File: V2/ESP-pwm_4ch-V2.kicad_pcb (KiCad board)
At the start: 2 copper layers, 103 x 67.8 mm, 37 parts, among them J1 12VDC, J2 OUT1, J3 OUT2, J4 OUT3, J5 OUT4, Q1 IRLB8721PBF, Q2 IRLB8721PBF, Q3 IRLB8721PBF, Q4 IRLB8721PBF, U1 L78M05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

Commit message: work in progress
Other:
- board text added: "MAX LOAD 5 A PER CHANNEL 16 A TOTAL"
- board text removed: "MAXIMUM 5 A PER CHANNEL 16 A TOTAL"
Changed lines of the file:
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@@
     (fp_arc (start -1.543104 -2.220356) (mid -0.831231 -1.810248) (end -0.550001 -1.038327) (layer "F.SilkS") (width 0.12))
     (fp_arc (start 5.549999 -1.038327) (mid 5.831229 -1.810249) (end 6.543103 -2.220357) (layer "F.SilkS") (width 0.12))
-    (fp_arc (start 0.549998 -1.038327) (mid -0.000002 1.174999) (end -0.550001 -1.038327) (layer "F.SilkS") (width 0.12))
+    (fp_arc (start 0.549998 -1.038327) (mid -0.000001 1.174999) (end -0.550001 -1.038327) (layer "F.SilkS") (width 0.12))
     (fp_arc (start -3.25 -5.15) (mid -2.5 -5.9) (end -1.75 -5.15) (layer "F.SilkS") (width 0.12))
     (fp_arc (start 3.456896 -2.220358) (mid 3.30859 -2.305797) (end 3.25 -2.466613) (layer "F.SilkS") (width 0.12))
@@
     (fp_arc (start 8.4 2.75) (mid 8.136396 3.386396) (end 7.5 3.65) (layer "F.CrtYd") (width 0.05))
     (fp_arc (start 5.4 -0.9) (mid 5.659303 -1.859555) (end 6.502666 -2.385599) (layer "F.CrtYd") (width 0.05))
-    (fp_arc (start 0.4 -0.9) (mid 0.000001 0.984885) (end -0.399999 -0.9) (layer "F.CrtYd") (width 0.05))
+    (fp_arc (start 0.4 -0.9) (mid 0 0.984886) (end -0.399999 -0.9) (layer "F.CrtYd") (width 0.05))
     (fp_arc (start 6.6 -5.2) (mid 7.5 -6.1) (end 8.4 -5.2) (layer "F.CrtYd") (width 0.05))
     (fp_line (start -3.099999 -5.1) (end -3.099999 -2.5) (layer "F.Fab") (width 0.1))
@@
     (fp_arc (start 1.75 -2.466613) (mid 1.69141 -2.305796) (end 1.543103 -2.220357) (layer "F.SilkS") (width 0.12))
     (fp_arc (start 0.549999 -1.038327) (mid 0.831229 -1.810249) (end 1.543103 -2.220357) (layer "F.SilkS") (width 0.12))
-    (fp_arc (start 0.549998 -1.038327) (mid -0.000002 1.174999) (end -0.550001 -1.038327) (layer "F.SilkS") (width 0.12))
+    (fp_arc (start 0.549998 -1.038327) (mid -0.000001 1.174999) (end -0.550001 -1.038327) (layer "F.SilkS") (width 0.12))
     (fp_arc (start 6.75 -5.149999) (mid 7.5 -5.899999) (end 8.25 -5.149999) (layer "F.SilkS") (width 0.12))
     (fp_arc (start -3.25 -5.15) (mid -2.5 -5.9) (end -1.75 -5.15) (layer "F.SilkS") (width 0.12))
@@
     (fp_arc (start -8.4 -5.2) (mid -7.5 -6.1) (end -6.6 -5.2) (layer "F.CrtYd") (width 0.05))
     (fp_arc (start 0.4 -0.9) (mid 0.659303 -1.859555) (end 1.502666 -2.385599) (layer "F.CrtYd") (width 0.05))
-    (fp_arc (start 0.4 -0.9) (mid 0.000001 0.984885) (end -0.399999 -0.9) (layer "F.CrtYd") (width 0.05))
+    (fp_arc (start 0.4 -0.9) (mid 0 0.984886) (end -0.399999 -0.9) (layer "F.CrtYd") (width 0.05))
     (fp_arc (start -4.6 -0.9) (mid -4.340697 -1.859555) (end -3.497334 -2.385599) (layer "F.CrtYd") (width 0.05))
     (fp_arc (start 5.4 -0.9) (mid 5.000001 0.984885) (end 4.600001 -0.9) (layer "F.CrtYd") (width 0.05))
@@
     (fp_arc (start 3.456896 -2.220358) (mid 3.30859 -2.305797) (end 3.25 -2.466613) (layer "F.SilkS") (width 0.12))
     (fp_arc (start 6.75 -2.466613) (mid 6.69141 -2.305796) (end 6.543103 -2.220357) (layer "F.SilkS") (width 0.12))
-    (fp_arc (start 0.549998 -1.038327) (mid -0.000002 1.174999) (end -0.550001 -1.038327) (layer "F.SilkS") (width 0.12))
+    (fp_arc (start 0.549998 -1.038327) (mid -0.000001 1.174999) (end -0.550001 -1.038327) (layer "F.SilkS") (width 0.12))
     (fp_arc (start -1.543103 -2.220357) (mid -1.69141 -2.305796) (end -1.75 -2.466613) (layer "F.SilkS") (width 0.12))
     (fp_arc (start -3.25 -5.15) (mid -2.5 -5.9) (end -1.75 -5.15) (layer "F.SilkS") (width 0.12))
@@
     (fp_arc (start -8.4 -5.2) (mid -7.5 -6.1) (end -6.6 -5.2) (layer "F.CrtYd") (width 0.05))
     (fp_arc (start -1.502666 -2.385599) (mid -0.659303 -1.859555) (end -0.4 -0.9) (layer "F.CrtYd") (width 0.05))
-    (fp_arc (start 0.4 -0.9) (mid 0.000001 0.984885) (end -0.399999 -0.9) (layer "F.CrtYd") (width 0.05))
+    (fp_arc (start 0.4 -0.9) (mid 0 0.984886) (end -0.399999 -0.9) (layer "F.CrtYd") (width 0.05))
     (fp_arc (start -4.6 -0.9) (mid -4.340697 -1.859555) (end -3.497334 -2.385599) (layer "F.CrtYd") (width 0.05))
     (fp_arc (start 0.4 -0.9) (mid 0.659303 -1.859555) (end 1.502666 -2.385599) (layer "F.CrtYd") (width 0.05))
@@
     (tags "capacitor tantalum")
     (property "Case" "1206/3216")
-    (property "JLCPCB BOM" "0")
-    (property "LCSC Part" "")
+    (property "JLCPCB BOM" "1")
+    (property "LCSC Part" "C7176")
     (property "Mfr" "AVX")
-    (property "Mfr PN" "TAJA105K035TNJ")
+    (property "Mfr PN" "TAJA105K035RNJ")
     (property "Sheetfile" "ESP-pwm_4ch-V2.kicad_sch")
     (property "Sheetname" "")
     (property "Technology" "Tantalum")
-    (property "Vendor" "Mouser")
-    (property "Vendor PN" "581-TAJA105K035TNJ")
+    (property "Vendor" "JLCPCB")
+    (property "Vendor PN" "C7176")
     (attr smd)
     (fp_text reference "C5" (at -3.81 0) (layer "F.SilkS")
@@
     (tags "SOIC SO")
     (property "Case" "SOIC-8")
-    (property "JLCPCB BOM" "0")
-    (property "LCSC Part" "")
+    (property "JLCPCB BOM" "1")
+    (property "LCSC Part" "C49058")
     (property "Mfr" "International Rectifier")
     (property "Mfr PN" "IR4427STRPBF\r")
     (property "Sheetfile" "ESP-pwm_4ch-V2.kicad_sch")
     (property "Sheetname" "")
-    (property "Vendor" "Mouser")
-    (property "Vendor PN" "942-IR4427STRPBF\r")
+    (property "Vendor" "JLCPCB")
+    (property "Vendor PN" "C49058")
     (attr smd)
     (fp_text reference "U4" (at 0 -3.4) (layer "F.SilkS")
@@
     (tags "SOIC SO")
     (property "Case" "SOIC-8")
-    (property "JLCPCB BOM" "0")
-    (property "LCSC Part" "")
+    (property "JLCPCB BOM" "1")
+    (property "LCSC Part" "C49058")
     (property "Mfr" "International Rectifier")
     (property "Mfr PN" "IR4427STRPBF\r")
     (property "Sheetfile" "ESP-pwm_4ch-V2.kicad_sch")
     (property "Sheetname" "")
-    (property "Vendor" "Mouser")
-    (property "Vendor PN" "942-IR4427STRPBF\r")
+    (property "Vendor" "JLCPCB")
+    (property "Vendor PN" "C49058")
     (attr smd)
     (fp_text reference "U5" (at 0 -3.4) (layer "F.SilkS")
@@
     (fp_arc (start 1.75 -2.466613) (mid 1.69141 -2.305796) (end 1.543103 -2.220357) (layer "F.SilkS") (width 0.12))
     (fp_arc (start -6.543104 -2.220357) (mid -5.831231 -1.810248) (end -5.550001 -1.038327) (layer "F.SilkS") (width 0.12))
-    (fp_arc (start 0.549998 -1.038327) (mid -0.000002 1.174999) (end -0.550001 -1.038327) (layer "F.SilkS") (width 0.12))
+    (fp_arc (start 0.549998 -1.038327) (mid -0.000001 1.174999) (end -0.550001 -1.038327) (layer "F.SilkS") (width 0.12))
     (fp_arc (start -1.543103 -2.220357) (mid -1.69141 -2.305796) (end -1.75 -2.466613) (layer "F.SilkS") (width 0.12))
     (fp_arc (start -4.450001 -1.038327) (mid -4.168771 -1.810249) (end -3.456897 -2.220357) (layer "F.SilkS") (width 0.12))
@@
     (fp_arc (start -1.509951 -2.38049) (mid -1.57415 -2.412895) (end -1.600006 -2.48) (layer "F.CrtYd") (width 0.05))
     (fp_arc (start -3.399994 -2.48) (mid -3.42585 -2.412895) (end -3.490049 -2.38049) (layer "F.CrtYd") (width 0.05))
-    (fp_arc (start 0.4 -0.9) (mid 0.000001 0.984885) (end -0.399999 -0.9) (layer "F.CrtYd") (width 0.05))
+    (fp_arc (start 0.4 -0.9) (mid 0 0.984886) (end -0.399999 -0.9) (layer "F.CrtYd") (width 0.05))
     (fp_arc (start 3.490049 -2.38049) (mid 3.42585 -2.412895) (end 3.399994 -2.48) (layer "F.CrtYd") (width 0.05))
     (fp_arc (start -6.502666 -2.385599) (mid -5.659303 -1.859555) (end -5.4 -0.9) (layer "F.CrtYd") (width 0.05))
@@
     (tags "capacitor tantalum")
     (property "Case" "1206/3216")
-    (property "JLCPCB BOM" "0")
-    (property "LCSC Part" "")
+    (property "JLCPCB BOM" "1")
+    (property "LCSC Part" "C7176")
     (property "Mfr" "AVX")
-    (property "Mfr PN" "TAJA105K035TNJ")
+    (property "Mfr PN" "TAJA105K035RNJ")
     (property "Sheetfile" "ESP-pwm_4ch-V2.kicad_sch")
     (property "Sheetname" "")
     (property "Technology" "Tantalum")
-    (property "Vendor" "Mouser")
-    (property "Vendor PN" "581-TAJA105K035TNJ")
+    (property "Vendor" "JLCPCB")
+    (property "Vendor PN" "C7176")
     (attr smd)
     (fp_text reference "C7" (at -3.81 0) (layer "F.SilkS")
@@
     (effects (font (size 1.5 1.5) (thickness 0.25)))
   )
-  (gr_text "MAXIMUM 5 A\nPER CHANNEL\n16 A TOTAL" (at 107.315 83.312) (layer "F.SilkS")
+  (gr_text "MAX LOAD 5 A\nPER CHANNEL\n16 A TOTAL" (at 107.315 83.312) (layer "F.SilkS")
     (effects (font (size 1.8 1.6) (thickness 0.3)))
   )

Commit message: wip
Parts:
- removed the REF** at (82.5, 125.7)
- added ?: , Tales:TMaschio_20x6.4mm, F.Cu at (108.0, 94.0)
- added REF**: OSHW-Logo2_14.6x12mm_SilkScreen, Symbol:OSHW-Logo2_14.6x12mm_SilkScreen, F.Cu at (108.0, 83.8)
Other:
- board text added: "MAX LOAD 5A/CHANNEL 16 A TOTAL"
- board text removed: "MAX LOAD 5 A PER CHANNEL 16 A TOTAL"

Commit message: General improvement to the routing
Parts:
- R4, R5, R6, R7: value 0R/0,125W/0805 -> 22R/0,125W/0805
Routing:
- net GNDREF: track 400.2 -> 405.9 mm
- net Net-(Q3-Pad1): track 18.5 -> 20.6 mm
- net Net-(Q1-Pad1): track 18.5 -> 20.6 mm

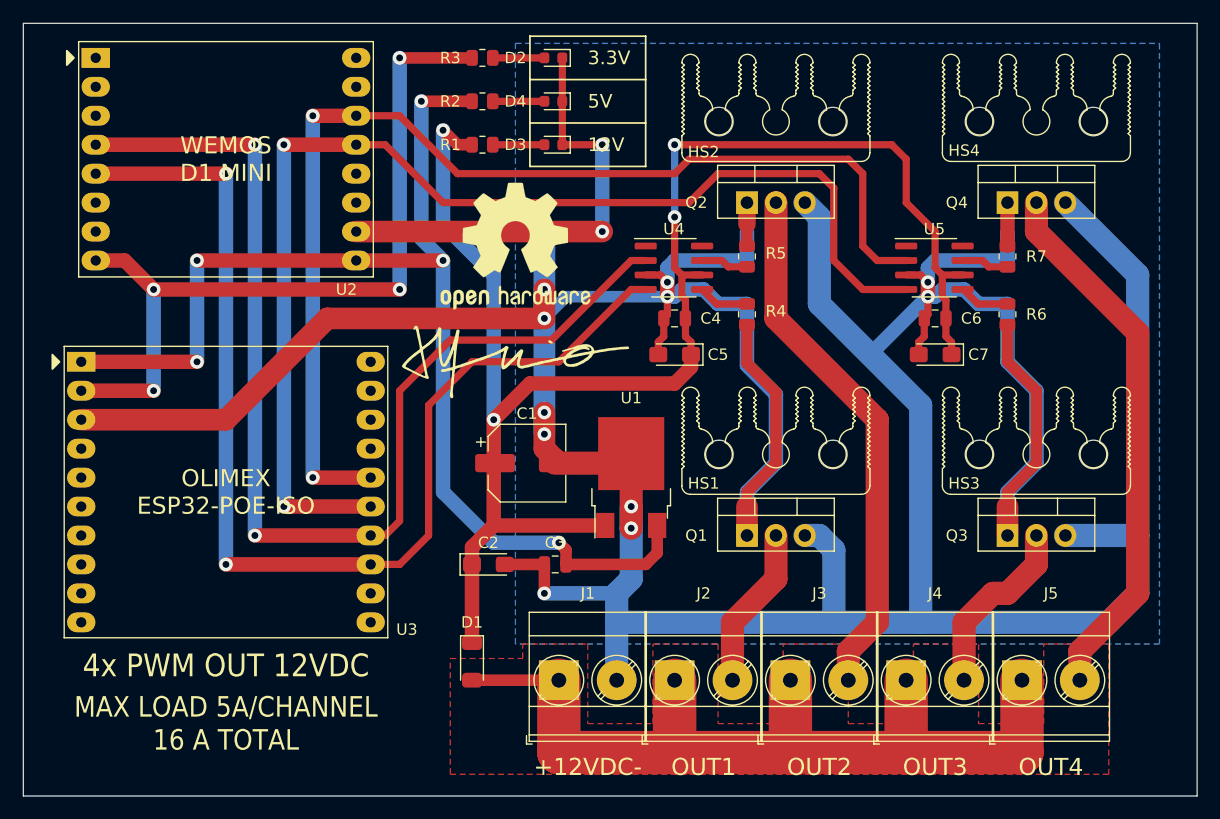
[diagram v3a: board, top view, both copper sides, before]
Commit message: Reset pulled up to +3.3V
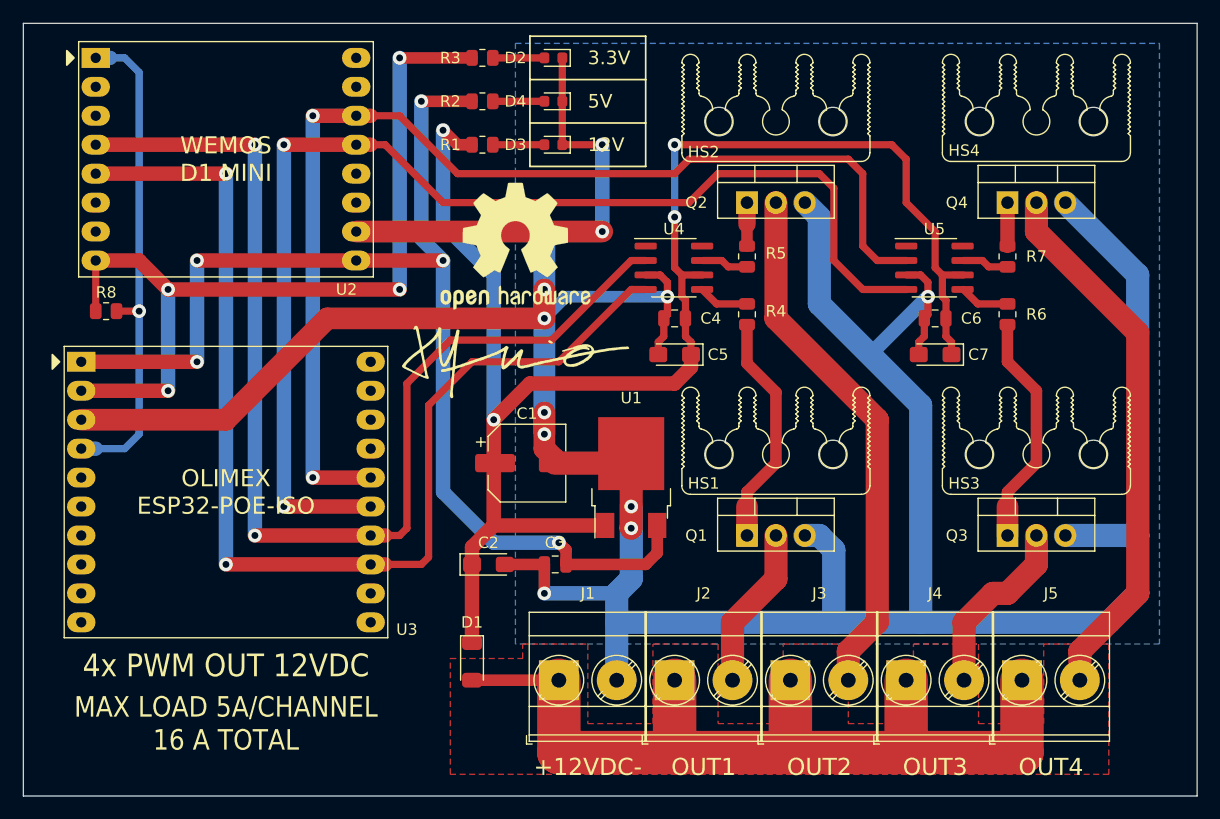
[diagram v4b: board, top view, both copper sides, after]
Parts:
- added R8: 4k7/0,125W/0805, Tales:R_0805_2012Metric, F.Cu at (72.0, 89.5)
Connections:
- U2 pad 1: unconnected-(U2-Pad1) -> Net-(U2-Pad1)
- U3 pad 4: unconnected-(U3-Pad4) -> Net-(U2-Pad1)
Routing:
- net GNDREF: track 405.9 -> 328.4 mm, vias 14 -> 12
- net Net-(U2-Pad1): track 0.00 -> 43.7 mm, vias 0 -> 1
- net +3V3: track 69.6 -> 75.3 mm
- net Net-(U2-Pad5): track 99.2 -> 100.4 mm
- net Net-(U2-Pad4): track 99.2 -> 100.0 mm

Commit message: Tweaking footprints
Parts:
- Q1, Q2, Q3, Q4: footprint Package_TO_SOT_THT:TO-220-3_Vertical -> Tales:TO-220-3_Vertical
- U4, U5: footprint Package_SO:SOIC-8_3.9x4.9mm_P1.27mm -> Tales:SOIC-8_3.9x4.9mm_P1.27mm

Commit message: PCB tweaks
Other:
- board text added: "+ CH1 -"
- board text added: "+ CH2 -"
- board text added: "+ CH3 -"
- board text added: "+ CH4 -"
- board text added: "MAX LOAD 5A/CHANNEL 16A TOTAL"
- board text removed: "MAX LOAD 5A/CHANNEL 16 A TOTAL"
- board text removed: "OUT1"
- board text removed: "OUT2"
- board text removed: "OUT3"
- board text removed: "OUT4"
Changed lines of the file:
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@@
     (fp_arc (start 6.75 -2.466613) (mid 6.691415 -2.305789) (end 6.543103 -2.220357) (layer "F.SilkS") (width 0.12))
     (fp_arc (start 3.456896 -2.220358) (mid 3.308595 -2.305798) (end 3.25 -2.466613) (layer "F.SilkS") (width 0.12))
-    (fp_arc (start 1.75 -2.466613) (mid 1.691411 -2.305794) (end 1.543103 -2.220357) (layer "F.SilkS") (width 0.12))
+    (fp_arc (start 1.75 -2.466613) (mid 1.691416 -2.305791) (end 1.543103 -2.220357) (layer "F.SilkS") (width 0.12))
     (fp_arc (start 5.549999 -1.038327) (mid 4.999999 1.174999) (end 4.45 -1.038327) (layer "F.SilkS") (width 0.12))
     (fp_arc (start 1.75 -5.15) (mid 2.5 -5.9) (end 3.25 -5.15) (layer "F.SilkS") (width 0.12))
@@
     (fp_arc (start 6.75 -5.149999) (mid 7.5 -5.899999) (end 8.25 -5.149999) (layer "F.SilkS") (width 0.12))
     (fp_arc (start -3.25 -2.466613) (mid -3.30859 -2.305796) (end -3.456897 -2.220357) (layer "F.SilkS") (width 0.12))
-    (fp_arc (start 1.75 -2.466613) (mid 1.691411 -2.305794) (end 1.543103 -2.220357) (layer "F.SilkS") (width 0.12))
+    (fp_arc (start 1.75 -2.466613) (mid 1.691416 -2.305791) (end 1.543103 -2.220357) (layer "F.SilkS") (width 0.12))
     (fp_arc (start -1.543104 -2.220356) (mid -0.831231 -1.810248) (end -0.550001 -1.038327) (layer "F.SilkS") (width 0.12))
     (fp_arc (start -4.450001 -1.038327) (mid -4.168771 -1.810249) (end -3.456897 -2.220357) (layer "F.SilkS") (width 0.12))
@@
     (fp_arc (start -3.25 -2.466613) (mid -3.30859 -2.305796) (end -3.456897 -2.220357) (layer "F.SilkS") (width 0.12))
     (fp_arc (start 5.549999 -1.038327) (mid 4.999999 1.174999) (end 4.45 -1.038327) (layer "F.SilkS") (width 0.12))
-    (fp_arc (start 1.75 -2.466613) (mid 1.691411 -2.305794) (end 1.543103 -2.220357) (layer "F.SilkS") (width 0.12))
+    (fp_arc (start 1.75 -2.466613) (mid 1.691416 -2.305791) (end 1.543103 -2.220357) (layer "F.SilkS") (width 0.12))
     (fp_arc (start 5.549999 -1.038327) (mid 5.831228 -1.81025) (end 6.543103 -2.220357) (layer "F.SilkS") (width 0.12))
     (fp_arc (start -6.543103 -2.220357) (mid -6.69141 -2.305796) (end -6.75 -2.466613) (layer "F.SilkS") (width 0.12))
@@
     (fp_arc (start -6.543103 -2.220357) (mid -6.69141 -2.305796) (end -6.75 -2.466613) (layer "F.SilkS") (width 0.12))
     (fp_arc (start -3.25 -5.15) (mid -2.5 -5.9) (end -1.75 -5.15) (layer "F.SilkS") (width 0.12))
-    (fp_arc (start 1.75 -2.466613) (mid 1.691411 -2.305794) (end 1.543103 -2.220357) (layer "F.SilkS") (width 0.12))
+    (fp_arc (start 1.75 -2.466613) (mid 1.691416 -2.305791) (end 1.543103 -2.220357) (layer "F.SilkS") (width 0.12))
     (fp_arc (start 8.24 2.75) (mid 8.02033 3.28033) (end 7.49 3.5) (layer "F.SilkS") (width 0.12))
     (fp_arc (start -6.543104 -2.220357) (mid -5.831231 -1.810248) (end -5.550001 -1.038327) (layer "F.SilkS") (width 0.12))
@@
   (gr_line (start 109.22 73.025) (end 119.38 73.025) (layer "F.SilkS") (width 0.15))
   (gr_line (start 109.22 65.405) (end 109.22 76.835) (layer "F.SilkS") (width 0.15))
+  (gr_line (start 139.7 128.27) (end 139.7 131.445) (layer "F.SilkS") (width 0.35))
+  (gr_line (start 160.02 128.27) (end 160.02 131.445) (layer "F.SilkS") (width 0.35))
+  (gr_line (start 149.86 128.27) (end 149.86 131.445) (layer "F.SilkS") (width 0.35))
+  (gr_line (start 129.54 128.27) (end 129.54 131.445) (layer "F.SilkS") (width 0.35))
+  (gr_line (start 109.22 128.27) (end 109.22 131.445) (layer "F.SilkS") (width 0.35))
+  (gr_line (start 119.38 128.27) (end 119.38 131.445) (layer "F.SilkS") (width 0.35))
   (gr_line (start 64.77 132.08) (end 167.77 132.08) (layer "Edge.Cuts") (width 0.1))
   (gr_line (start 167.77 64.28) (end 64.77 64.28) (layer "Edge.Cuts") (width 0.1))
   (gr_line (start 167.77 132.08) (end 167.77 64.28) (layer "Edge.Cuts") (width 0.1))
   (gr_line (start 64.77 64.28) (end 64.77 132.08) (layer "Edge.Cuts") (width 0.1))
-  (gr_text "OUT2" (at 134.62 129.54) (layer "F.SilkS")
-    (effects (font (size 1.5 1.5) (thickness 0.25)))
-  )
-  (gr_text "OUT1" (at 124.46 129.54) (layer "F.SilkS")
-    (effects (font (size 1.5 1.5) (thickness 0.25)))
-  )
-  (gr_text "OUT3" (at 144.78 129.54) (layer "F.SilkS")
-    (effects (font (size 1.5 1.5) (thickness 0.25)))
-  )
-  (gr_text "OUT4" (at 154.94 129.54) (layer "F.SilkS")
-    (effects (font (size 1.5 1.5) (thickness 0.25)))
+  (gr_text "+ CH1 -" (at 124.46 129.54) (layer "F.SilkS")
+    (effects (font (size 1.5 1.1) (thickness 0.25)))
   )
   (gr_text "+12VDC-" (at 114.3 129.54) (layer "F.SilkS")
-    (effects (font (size 1.5 1.5) (thickness 0.25)))
+    (effects (font (size 1.5 1.1) (thickness 0.25)))
   )
   (gr_text "4x PWM OUT 12VDC" (at 82.55 120.65) (layer "F.SilkS")
@@
     (effects (font (size 1.5 1.5) (thickness 0.25)))
   )
-  (gr_text "MAX LOAD 5A/CHANNEL\n16 A TOTAL" (at 82.55 125.73) (layer "F.SilkS")
+  (gr_text "MAX LOAD 5A/CHANNEL\n16A TOTAL" (at 82.55 125.73) (layer "F.SilkS")
     (effects (font (size 1.8 1.6) (thickness 0.3)))
   )
+  (gr_text "+ CH2 -" (at 134.62 129.54) (layer "F.SilkS")
+    (effects (font (size 1.5 1.1) (thickness 0.25)))
+  )
+  (gr_text "+ CH4 -" (at 154.94 129.54) (layer "F.SilkS")
+    (effects (font (size 1.5 1.1) (thickness 0.25)))
+  )
+  (gr_text "+ CH3 -" (at 144.78 129.54) (layer "F.SilkS")
+    (effects (font (size 1.5 1.1) (thickness 0.25)))
+  )
   (gr_text "SUPORTES PCI METALTEX SP7\n1x pé macho  9 mm\n1x pé fêmea 9 mm\n2x espaçador 20 mm\n1x espaçador 45 mm\nComprimento total 103 mm\nLargura da placa 67,8 mm" (at 170.18 71.12) (layer "Cmts.User")
